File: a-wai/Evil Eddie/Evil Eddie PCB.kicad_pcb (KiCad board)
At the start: 2 copper layers, 280 x 120 mm, 97 parts, among them K1 G5V2, P1 RLY+, P11 Ug2, P14 EARTH, P15 LD GND, P16 CLN EQ GND, P17 LD EQ, P2 RLY-, P4 CLN EQ, P6 FROM LD EQ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

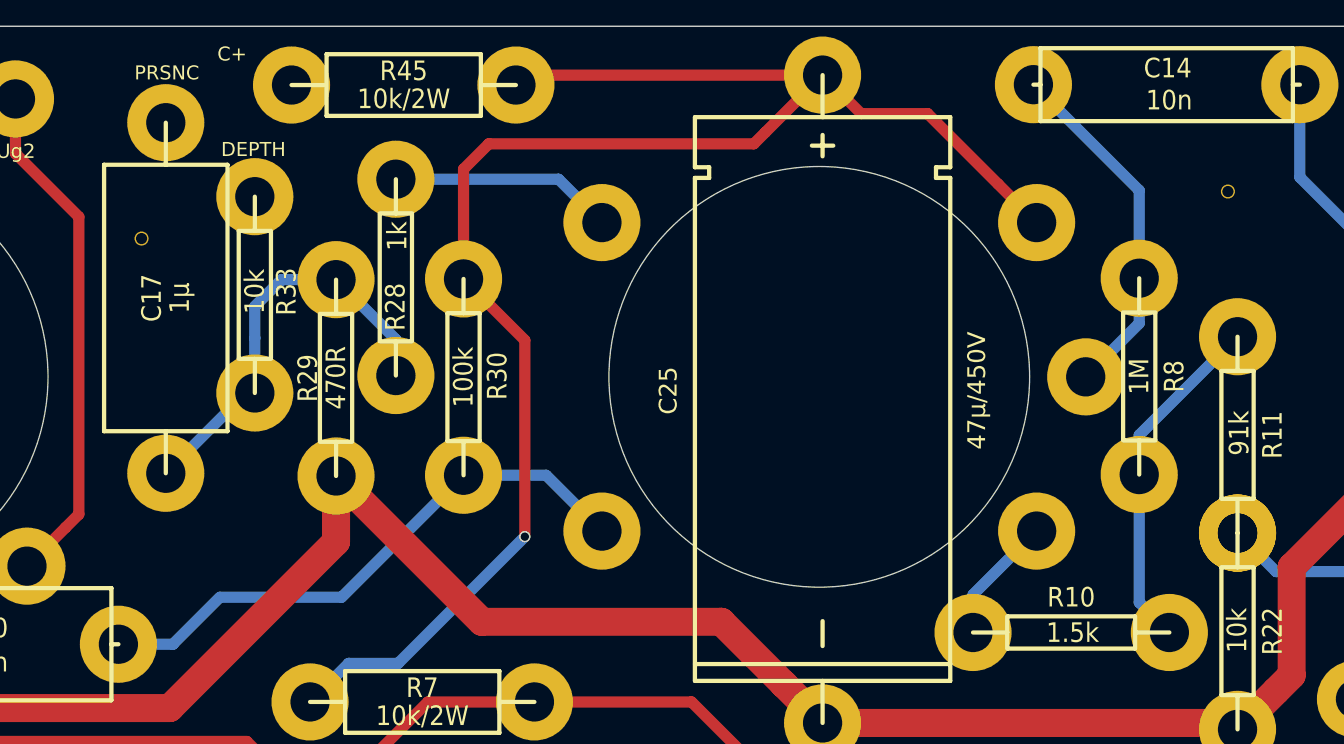
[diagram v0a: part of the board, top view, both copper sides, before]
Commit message: Update Evil Eddie Schematics & PCB
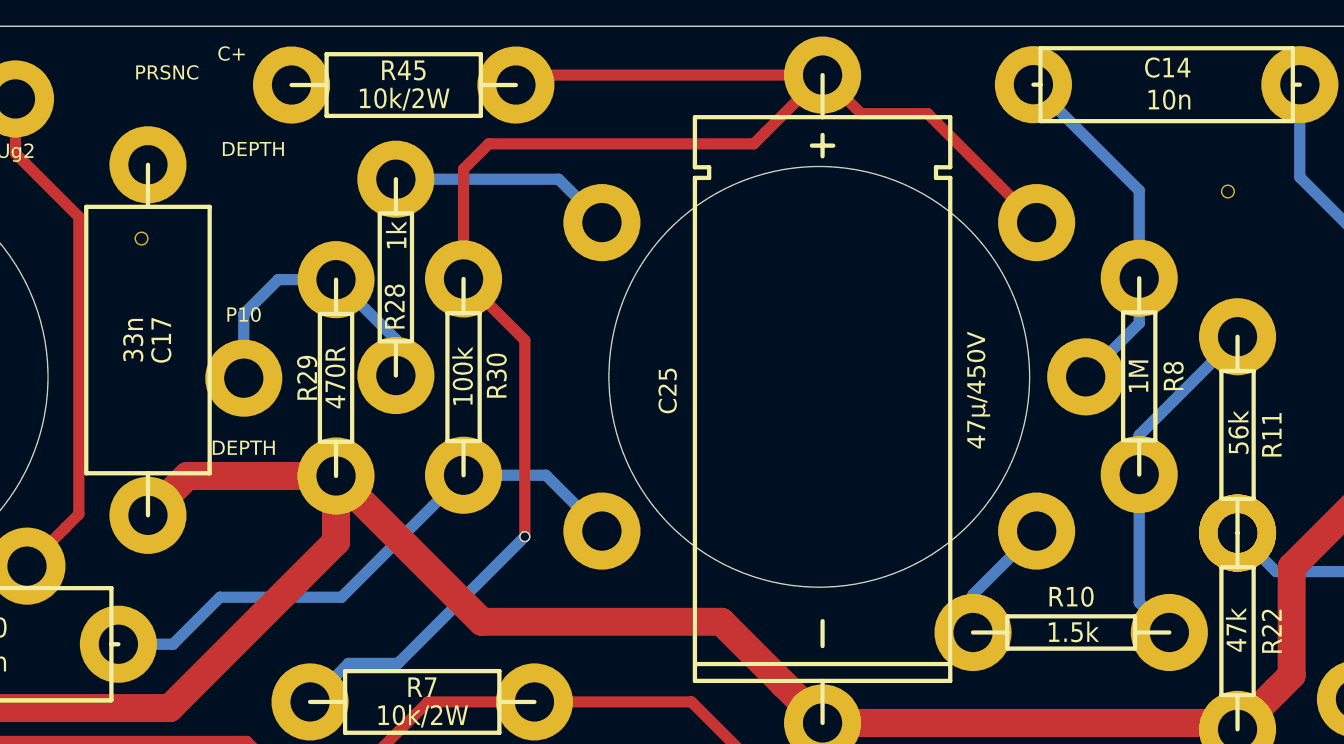
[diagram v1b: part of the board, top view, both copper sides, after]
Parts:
- removed R33: 10k, A-wai_Turrets:R_0.5W
- added P10: DEPTH, A-wai_Turrets:TURRET, F.Cu at (169.0, 125.1)
- C17: value 1µ -> 33n
- R11: value 91k -> 56k
- R22: value 10k -> 47k
- moved C17 3.26 mm to (162.1, 122.4), turned to 270 degrees
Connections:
- C1 pad 1: F+ -> Net-(C1-Pad1)
- C17 pad 2: Net-(C17-Pad2) -> GND
- C2 pad 1: E+ -> Net-(C2-Pad1)
- C24 pad 1: G+ -> Net-(C24-Pad1)
- C25 pad 1: C+ -> Net-(C25-Pad1)
- C4 pad 1: D+ -> Net-(C4-Pad1)
- K1 pad 11: Net-(K1-Pad11) -> (no net)
- K1 pad 8: Net-(K1-Pad8) -> (no net)
- K1 pad 9: Net-(K1-Pad9) -> (no net)
- P6 pad 1: Net-(K1-Pad8) -> (no net)
- R13 pad 1: F+ -> (no net)
- R18 pad 1: E+ -> (no net)
- R19 pad 1: G+ -> (no net)
- R2 pad 1: E+ -> Net-(C2-Pad1)
- R2 pad 2: F+ -> Net-(C1-Pad1)
- R24 pad 1: E+ -> (no net)
- R28 pad 2: Net-(C17-Pad1) -> Net-(P10-Pad1)
- R29 pad 1: Net-(C17-Pad1) -> Net-(P10-Pad1)
- R3 pad 1: G+ -> (no net)
- R30 pad 1: C+ -> (no net)
- R32 pad 1: D+ -> (no net)
- R39 pad 1: D+ -> (no net)
- R4 pad 1: D+ -> Net-(C4-Pad1)
- R4 pad 2: E+ -> Net-(C2-Pad1)
- R44 pad 1: D+ -> Net-(C4-Pad1)
- R44 pad 2: G+ -> Net-(C24-Pad1)
- R45 pad 2: C+ -> Net-(C25-Pad1)
- R6 pad 1: F+ -> (no net)
- R7 pad 1: C+ -> Net-(C25-Pad1)
- R7 pad 2: D+ -> Net-(C4-Pad1)
- U1 pad 2: Net-(K1-Pad9) -> (no net)
- U2 pad 2: Net-(K1-Pad11) -> (no net)
- U5 pad 6: C+ -> (no net)
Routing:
- net Net-(C4-Pad1): track 0.00 -> 254.6 mm
- net D+: track 254.6 -> 0.00 mm
- net (no net): track 0.62 -> 200.9 mm, vias 0 -> 2
- net Net-(K1-Pad11): track 127.4 -> 0.00 mm, vias 1 -> 0
- net Net-(C25-Pad1): track 0.00 -> 118.4 mm, vias 0 -> 1
- net C+: track 118.4 -> 0.00 mm, vias 1 -> 0
- net Net-(C2-Pad1): track 0.00 -> 114.3 mm
- net E+: track 114.3 -> 0.00 mm
- net Net-(C1-Pad1): track 0.00 -> 67.9 mm
- net F+: track 67.9 -> 0.00 mm
- net Net-(K1-Pad9): track 67.1 -> 0.00 mm, vias 1 -> 0
- net Net-(C24-Pad1): track 0.00 -> 59.1 mm
- net G+: track 59.1 -> 0.00 mm
- net Net-(C17-Pad1): track 30.1 -> 0.00 mm
- net Net-(P10-Pad1): track 0.00 -> 20.8 mm
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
